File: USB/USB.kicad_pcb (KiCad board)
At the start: 4 copper layers, 70 x 60 mm, 20 parts, among them J1 USBC-4-0-CX90MW9-24P1, U1 TVS-choke-2-pair-EMI8142MUTAG, U2 ESDA25L, U3 USB SWITCH 2CHANNEL TS3USB221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, U5 TVS-choke-2-pair-EMI8142MUTAG, U6 usb-polarity-TUSB321RWBR, U7 MUX HD3SS460RHRR

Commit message: RX1 line problem
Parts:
- moved U2 54.1 mm to (120.0, 83.0)
- moved U7 19.2 mm to (109.0, 86.7)
- moved U5 6.55 mm to (113.5, 85.2)
- moved U1 5.33 mm to (118.5, 92.1), turned to 180 degrees
- moved U4 5.00 mm to (111.5, 96.0)
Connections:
- U7 pad 1: RX2+f -> RX1+f
- U7 pad 10: RX1-f -> RX2-f
- U7 pad 2: RX2-f -> RX1-f
- U7 pad 9: RX1+f -> RX2+f
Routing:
- net RX1+: track 0.00 -> 5.65 mm
- net RX2+f: track 0.00 -> 1.90 mm

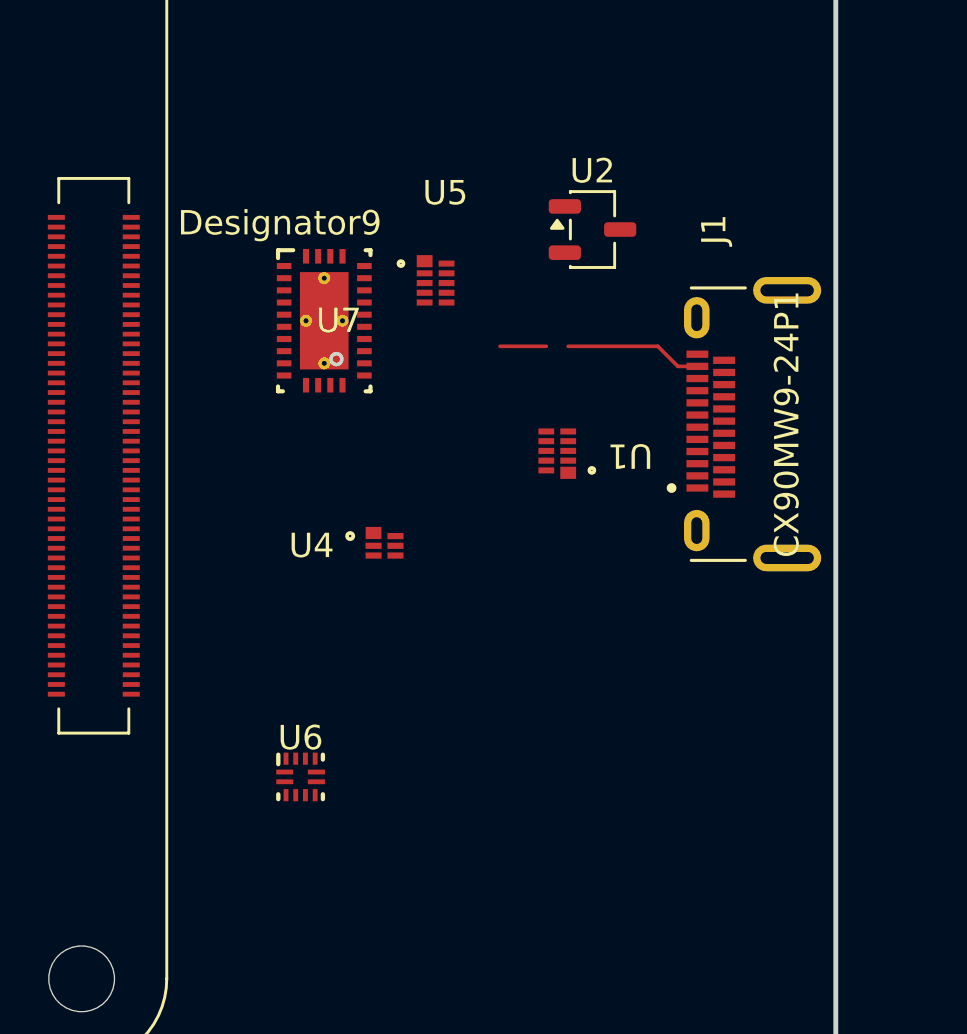
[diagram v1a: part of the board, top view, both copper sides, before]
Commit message: TVS chokes connected
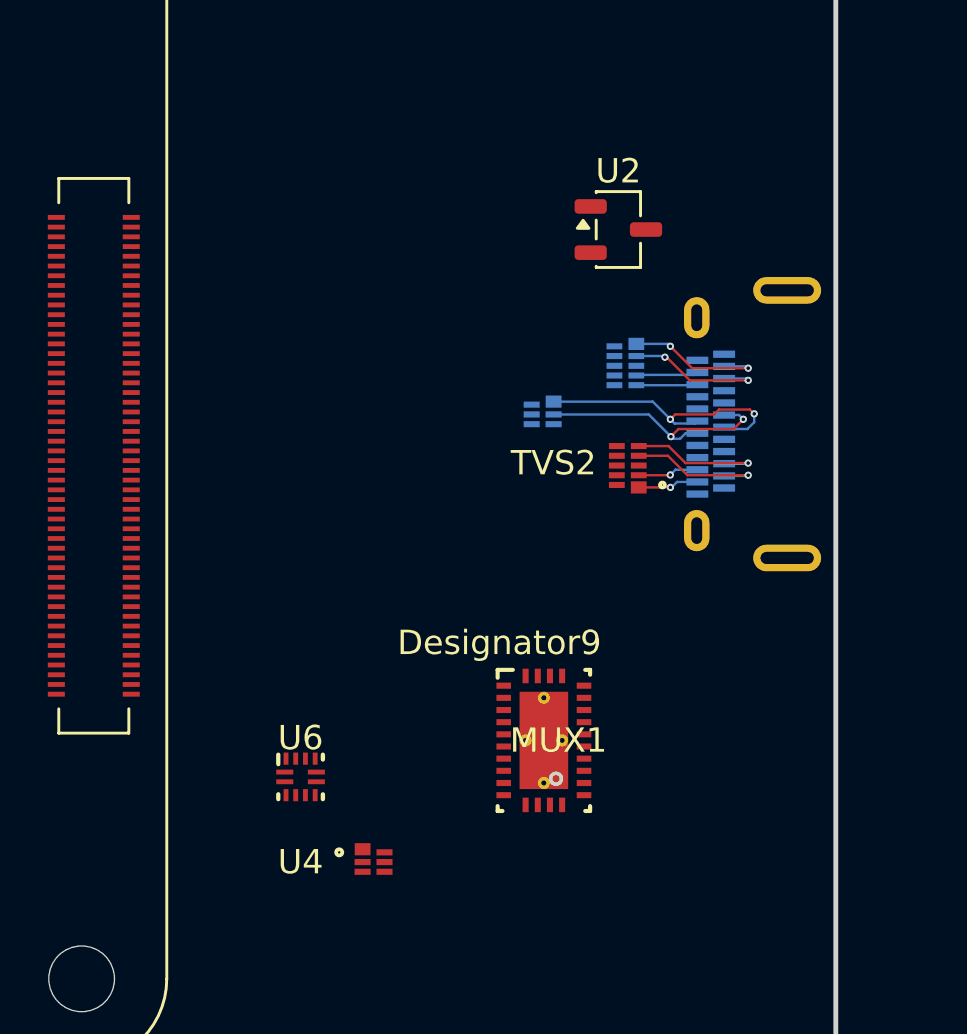
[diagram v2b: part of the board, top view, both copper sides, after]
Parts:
- removed U1, U5: TVS-choke-2-pair-EMI8142MUTAG, SPIRIT-footprints:2-channel-TVS-chokeXDFN10_2P2X1P3_ONS
- removed U7: MUX HD3SS460RHRR, SPIRIT-footprints:USB-MUX-RHR0028A
- added MUX1: MUX HD3SS460RHRR, SPIRIT-footprints:USB-MUX-RHR0028A, F.Cu at (118.0, 104.0)
- added TVS1: TVS-choke-2-pair-EMI8142MUTAG, SPIRIT-footprints:2-channel-TVS-chokeXDFN10_2P2X1P3_ONS, B.Cu at (121.3, 88.6)
- added TVS2: TVS-choke-2-pair-EMI8142MUTAG, SPIRIT-footprints:2-channel-TVS-chokeXDFN10_2P2X1P3_ONS, F.Cu at (121.5, 92.7)
- added TVS3: ~, SPIRIT-footprints:1-channel-TVS-choke-XDFN6_1P2X1P2_ONS, B.Cu at (118.0, 90.6)
- J1: moved to B.Cu
- moved U4 13.0 mm to (111.0, 109.0)
- moved U2 1.06 mm to (121.1, 83.0)
- turned J1 to -90 degrees
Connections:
- C1 pad 2: RX1- -> SSTR2-
- C2 pad 2: RX1+ -> SSTR2+
- C3 pad 2: TX1- -> SSTX2-
- C4 pad 2: TX1+ -> SSTX2+
- J1 pad A10: RX1- -> RX2-
- J1 pad A11: RX1+ -> RX2+
- J1 pad B2: TX1+ -> TX2+
- J1 pad B3: TX1- -> TX2-
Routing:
- net D+: track 0.00 -> 11.7 mm, vias 0 -> 2
- net D-: track 0.00 -> 10.6 mm, vias 0 -> 2
- net RX1-: track 0.00 -> 6.04 mm, vias 0 -> 2
- net TX2+: track 0.00 -> 5.83 mm, vias 0 -> 1
- net TX2-: track 0.00 -> 5.79 mm, vias 0 -> 1
- net TX1+: track 0.00 -> 2.56 mm
- net TX1-: track 0.00 -> 2.52 mm
- net RX2-: track 0.00 -> 2.50 mm, vias 0 -> 1
- net RX2+: track 0.00 -> 2.50 mm, vias 0 -> 1
- net RX2+f: track 1.90 -> 0.00 mm
- net RX1+: track 5.65 -> 6.04 mm, vias 0 -> 2

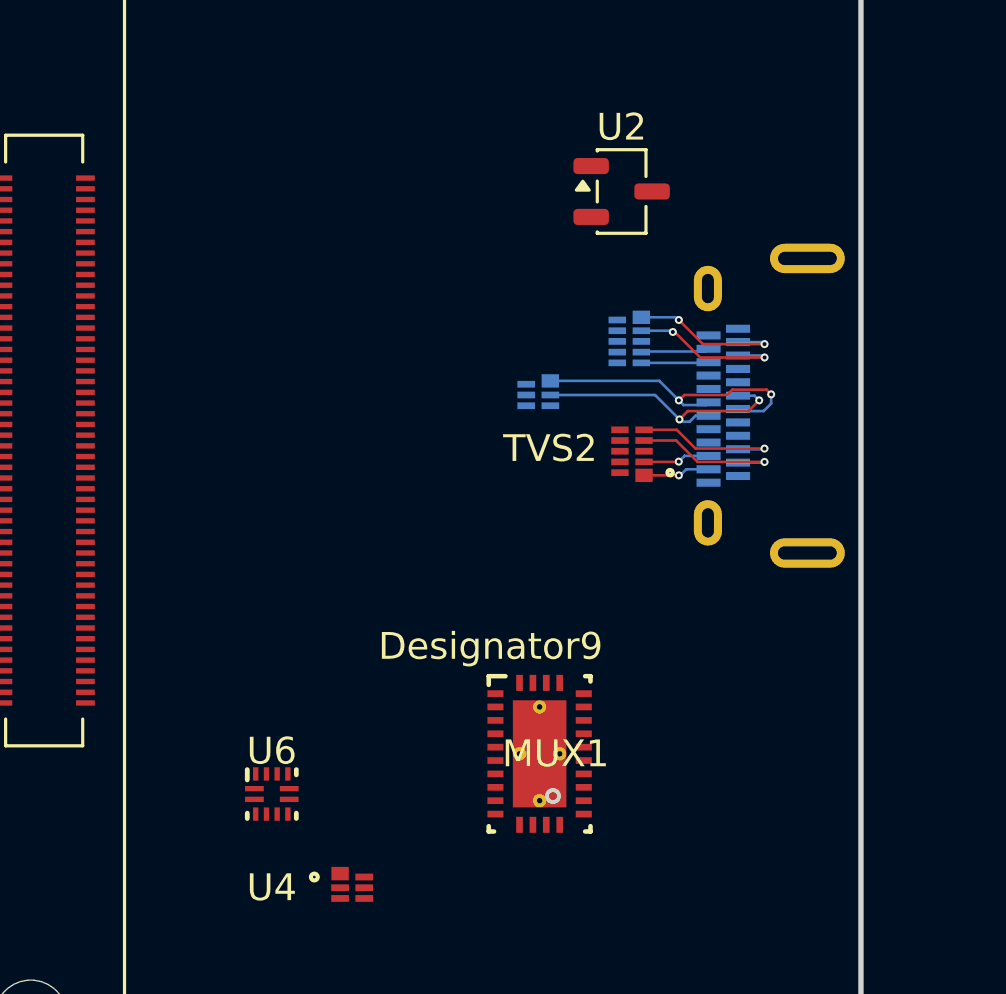
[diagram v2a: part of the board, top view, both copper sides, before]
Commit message: reroute data lines for Zd
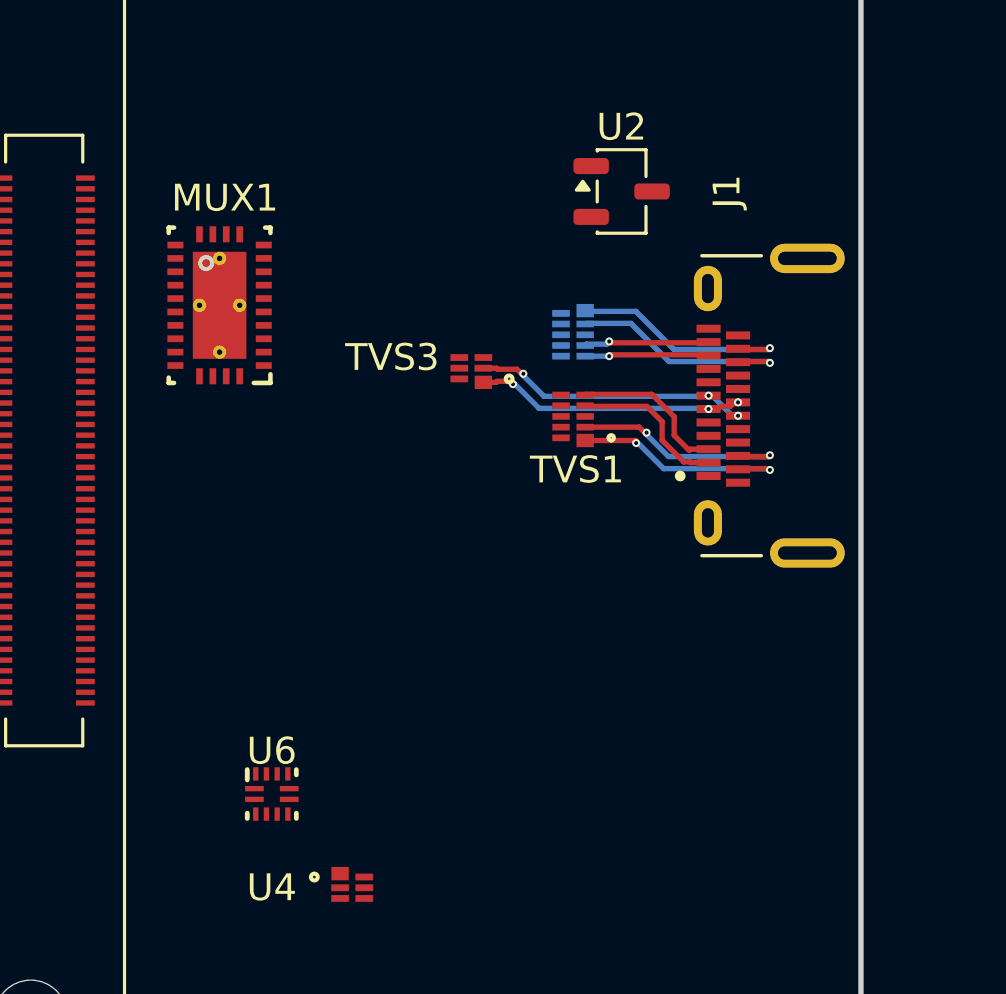
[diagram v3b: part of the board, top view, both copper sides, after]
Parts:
- J1, TVS1, TVS3: moved to F.Cu
- TVS2: moved to B.Cu
- moved MUX1 20.6 mm to (106.0, 87.2), turned to 180 degrees
- moved TVS2 4.87 mm to (119.2, 88.3)
- moved TVS1 3.50 mm to (119.2, 91.4)
- moved TVS3 2.69 mm to (115.4, 89.6)
- turned J1 to 90 degrees
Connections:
- net RX1+f renamed RX1f+
- net TX1+f renamed TX1f+
- MUX1 pad 10: RX2-f -> RX2f-
- MUX1 pad 2: RX1-f -> TX1f-
- MUX1 pad 5: TX1-f -> RX1f-
- MUX1 pad 6: TX2+f -> TX2f+
- MUX1 pad 7: TX2-f -> TX2f-
- MUX1 pad 9: RX2+f -> RX2f+
- TVS1 pad 6: TX1-f -> TX1f-
- TVS1 pad 9: RX1-f -> RX1f-
- TVS2 pad 1: RX2+ -> TX2+
- TVS2 pad 10: RX2+f -> TX2f+
- TVS2 pad 2: RX2- -> TX2-
- TVS2 pad 4: TX2+ -> RX2+
- TVS2 pad 5: TX2- -> RX2-
- TVS2 pad 6: TX2-f -> RX2f-
- TVS2 pad 7: TX2+f -> RX2f+
- TVS2 pad 9: RX2-f -> TX2f-
- TVS3 pad 5: D-f -> Df-
- TVS3 pad 6: D+f -> Df+
- U3 pad 7: D-f -> Df-
- U3 pad 8: D+f -> Df+
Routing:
- net TX1-: track 2.52 -> 5.90 mm
- net TX1+: track 2.56 -> 5.90 mm
- net TX2-: track 5.79 -> 8.74 mm
- net TX2+: track 5.83 -> 8.74 mm
- net RX1-: track 6.04 -> 8.64 mm
- net RX1+: track 6.04 -> 8.55 mm
- net RX2+: track 2.50 -> 4.70 mm
- net RX2-: track 2.50 -> 4.64 mm
- net D+: track 11.7 -> 10.1 mm, vias 2 -> 3
- net D-: track 10.6 -> 10.3 mm, vias 2 -> 3

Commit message: progress
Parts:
- removed C1, C2, C3, C4: 0.33 µF coupling cap, SPIRIT-footprints:USBC_capacitor_CAPC0603X33N
- removed U4: ~, SPIRIT-footprints:1-channel-TVS-choke-XDFN6_1P2X1P2_ONS
- added ?: , , F.Cu at (128.0, 98.2)
- added G***: LOGO, LOGO, F.Cu at (127.5, 65.8)
- added J2: ~, Connector_PinHeader_1.00mm:PinHeader_1x02_P1.00mm_Vertical, F.Cu at (120.6, 99.8)
- added J3: ~, Connector_PinHeader_1.00mm:PinHeader_1x02_P1.00mm_Vertical, F.Cu at (120.6, 96.2)
- moved U3 61.2 mm to (110.2, 82.1)
- moved U6 11.6 mm to (116.8, 98.0), turned to 180 degrees
- moved TVS3 5.71 mm to (115.1, 83.9)
- moved MUX1 5.55 mm to (111.0, 89.8)
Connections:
- MUX1 pad 2: TX1f- -> RX1f-
- MUX1 pad 5: RX1f- -> TX1f-
- Module1 pad 157: Net-(Module1B-USB3-1-RX_N) -> SSTR2-
- Module1 pad 159: Net-(Module1B-USB3-1-RX_P) -> SSTR2+
- Module1 pad 169: Net-(Module1B-USB3-1-TX_N) -> SSTX2-
- Module1 pad 171: Net-(Module1B-USB3-1-TX_P) -> SSTX2+
- U6 pad 1: CC1 -> Net-(U6-CC1)
- U6 pad 2: CC2 -> Net-(U6-CC2)
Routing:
- net SSTR2+: track 0.00 -> 20.2 mm, vias 0 -> 2
- net SSTR2-: track 0.00 -> 20.1 mm, vias 0 -> 2
- net SSTX2+: track 0.00 -> 20.0 mm, vias 0 -> 2
- net SSTX2-: track 0.00 -> 19.9 mm, vias 0 -> 2
- net MUX POL: track 0.00 -> 14.2 mm, vias 0 -> 2
- net CC2: track 0.00 -> 13.7 mm
- net CC1: track 0.00 -> 12.6 mm, vias 0 -> 2
- net TX2f+: track 0.00 -> 10.4 mm, vias 0 -> 3
- net TX2f-: track 0.00 -> 9.75 mm, vias 0 -> 3
- net RX2f-: track 0.00 -> 7.21 mm, vias 0 -> 3
- net RX2f+: track 0.00 -> 6.51 mm, vias 0 -> 1
- net TX1f-: track 0.00 -> 6.41 mm
- net TX1f+: track 0.00 -> 6.39 mm
- net RX1f-: track 0.00 -> 6.28 mm
- net RX1f+: track 0.00 -> 6.24 mm
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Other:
- outline, holes or cut-outs redrawn
- board text added: "EMC compliance? Never heard of her."
- board text added: "WELCOME TO USB HELL"
- board text added: "make this a tented via so there is no short to the connector which is GND"

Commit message: usb: second attempt at layout
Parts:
- TVS2: moved to F.Cu
- moved R4 53.4 mm to (113.4, 87.2), turned to 90 degrees
- moved R3 49.9 mm to (117.1, 87.2), turned to 90 degrees
- moved R2 48.0 mm to (115.6, 87.2), turned to 90 degrees
- moved R1 47.3 mm to (106.9, 92.2), turned to 180 degrees
- moved C7 41.4 mm to (110.3, 94.4), turned to -90 degrees
- moved C6 40.1 mm to (108.9, 94.4), turned to -90 degrees
- moved C5 36.9 mm to (112.1, 93.6), turned to -90 degrees
- moved J2 18.9 mm to (111.7, 83.1)
- moved U3 17.8 mm to (117.6, 98.2), turned to 180 degrees
- moved J3 17.3 mm to (109.3, 83.1)
- moved TVS3 14.6 mm to (121.5, 97.0)
- moved U6 9.76 mm to (109.8, 91.2)
- moved MUX1 4.50 mm to (115.1, 91.6)
- moved U2 2.38 mm to (121.8, 80.7)
- moved TVS2 1.81 mm to (119.0, 90.2)
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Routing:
- net SYS D-: track 0.00 -> 27.2 mm, vias 0 -> 2
- net SYS D+: track 0.00 -> 25.9 mm, vias 0 -> 2
- net GND: track 1.70 -> 14.4 mm, vias 0 -> 18
- net CC2: track 13.7 -> 25.8 mm
- net TX2f+: track 10.4 -> 2.03 mm, vias 3 -> 0
- net TX2f-: track 9.75 -> 1.99 mm, vias 3 -> 0
- net Df-: track 0.00 -> 6.75 mm, vias 0 -> 2
- net Df+: track 0.00 -> 6.71 mm, vias 0 -> 2
- net USBC POW: track 0.00 -> 5.46 mm, vias 0 -> 4
- net RX2f-: track 7.21 -> 1.91 mm, vias 3 -> 0
- net Net-(U6-CC2): track 3.40 -> 8.21 mm
- net Net-(MUX1-AMSEL): track 0.00 -> 4.65 mm, vias 0 -> 2
- net RX2f+: track 6.51 -> 1.95 mm, vias 1 -> 0
- net TX1f+: track 6.39 -> 2.00 mm
- net TX1f-: track 6.41 -> 2.02 mm
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
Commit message: update to kicad 10
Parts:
- moved G*** 21.9 mm to (105.7, 66.1)
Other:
- board text added: "V ELECTRONICS"
